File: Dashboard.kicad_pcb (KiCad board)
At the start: 2 copper layers, 176.5 x 121.5 mm, 160 parts, among them J1 Left_Signal, J10 AccelConn, J11 BrakeConn, J12 AccelConn2, J13 BrakeConn2, J14 Motor-P, J15 Motor-C, J16 Array-C, J17 Array-P, J18 PowerConn, J19 CAN_OUT, J2 Right_Signal, J20 MotorCANConnector, J21 CAN_IN, J22 CAN_OUT, J23 USB_B_Micro, J24 ExtraGPIO_Conn, J25 UART_TP, J26 CAN_TP, J27 CAN_TP, J3 Brake Light, J4 Headlight, J5 MinionConn, J6 SPI, J7 BPS_PWR, J8 JTAG, SW10 RESET, SW8 SW_Rotary2x6, SW9 KILL_SW, U1 EL3H7, U10 EL3H7, U11 EL3H7, U12 RI3-1205S, U13 NCP1117-3.3_SOT223, U14 ADM3055E, U15 CDSOT23-T24CAN, U16 LTC6820, U17 ADM3055E, U18 CDSOT23-T24CAN, U19 CP2102N-A01-GQFN24, U2 EL3H7, U20 HX1188FNL, U3 EL3H7, U4 EL3H7, U5 EL3H7, U6 EL3H7, U7 STM32F413RHTx, U8 EL3H7, U9 EL3H7, Y1 Crystal

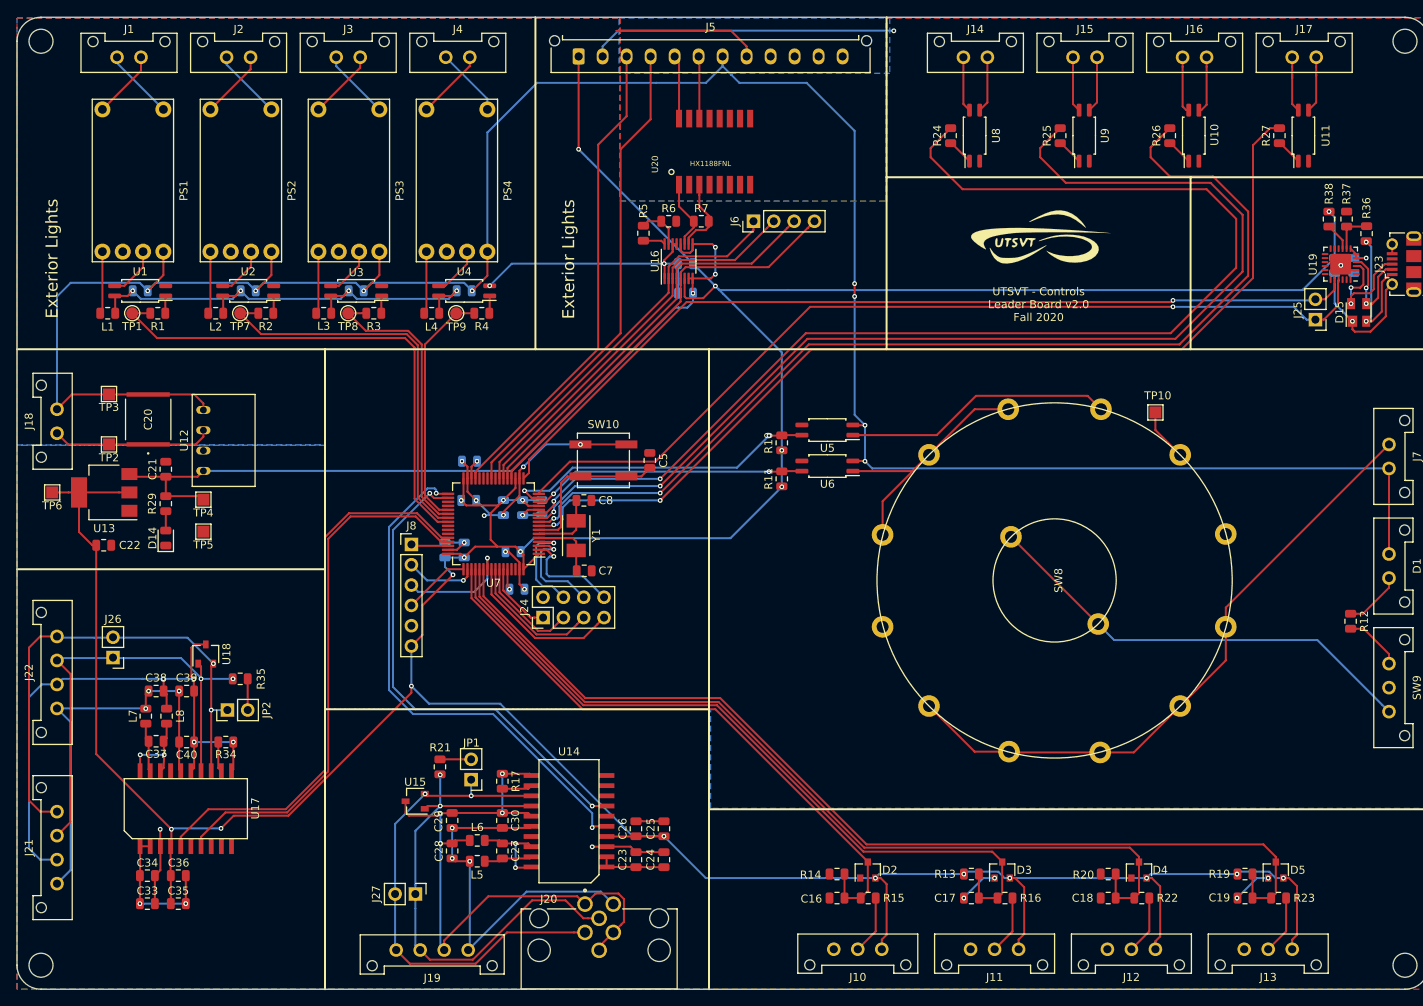
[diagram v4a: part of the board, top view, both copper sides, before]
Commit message: Labels sections and fixes DRC errors
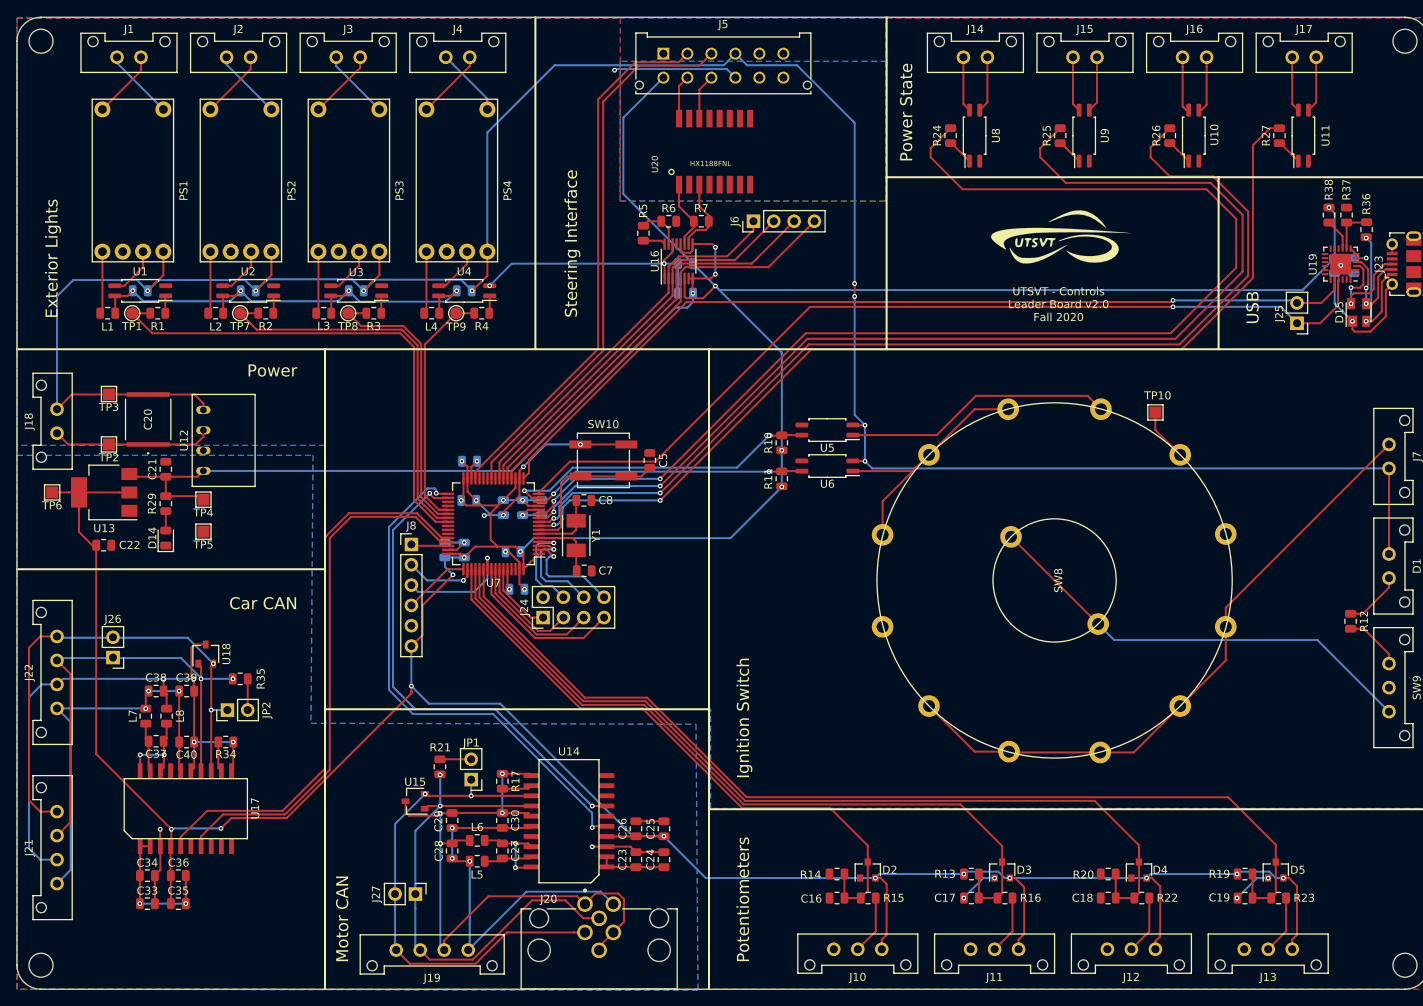
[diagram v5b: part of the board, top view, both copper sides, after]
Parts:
- J5: footprint Connector_Molex:Molex_Micro-Fit_3.0_43650-1215_1x12_P3.00mm_Vertical -> UTSVT_Connectors:Molex_MicroFit3.0_2x6xP3.00mm_PolarizingPeg_Vertical
- moved J5 10.6 mm to (111.8, 58.0)
- moved LOGO2 2.50 mm to (161.2, 81.1)
- moved J25 2.34 mm to (191.0, 91.8)
- moved R36 0.50 mm to (199.7, 80.0)
- moved R37 0.50 mm to (197.2, 78.2)
- moved R38 0.50 mm to (195.0, 78.2)
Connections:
- J5 pad 1: +3V3 -> +12V
- J5 pad 10: Net-(J5-Pad10) -> GND
- J5 pad 2: +12V -> /UART3_Tx
- J5 pad 3: /UART3_Tx -> /UART3_Rx
- J5 pad 4: /UART3_Rx -> GNDPWR
- J5 pad 7: GNDPWR -> +3V3
- J5 pad 8: GND -> Net-(J5-Pad8)
- U20 pad 14: Net-(J5-Pad6) -> Net-(J5-Pad9)
- U20 pad 16: Net-(J5-Pad5) -> Net-(J5-Pad8)
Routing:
- net +12V: track 120.3 -> 82.6 mm, vias 5 -> 4
- net Net-(J5-Pad5): track 8.00 -> 0.00 mm
- net /UART3_Rx: track 61.0 -> 68.9 mm
- net Net-(J5-Pad6): track 7.81 -> 0.00 mm
- net /UART3_Tx: track 60.6 -> 67.3 mm
- net Net-(J5-Pad9): track 0.00 -> 5.75 mm
- net Net-(J5-Pad8): track 0.00 -> 5.56 mm
- net GND: track 163.4 -> 160.6 mm, vias 20 -> 21
- net +3V3: track 533.1 -> 530.5 mm, vias 22 -> 21
- net GNDPWR: track 303.2 -> 305.2 mm
- net /Accel_Pot: track 76.7 -> 78.0 mm
- net /Brake_Pot: track 93.2 -> 94.4 mm
- net /Brake_Pot2: track 126.6 -> 127.5 mm
- net /Accel_Pot2: track 110.1 -> 111.0 mm
- net Net-(R38-Pad2): track 3.46 -> 3.96 mm
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- removed copper zone on B.Cu, net (none)
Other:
- net class Default: clearance 0.2 -> 0.127
- rule trace_clearance: 0.2 -> 0.127
- board text added: "Car CAN"
- board text added: "Ignition Switch"
- board text added: "Motor CAN"
- board text added: "Potentiometers"
- board text added: "Power"
- board text added: "Power State"
- board text added: "Steering Interface"
- board text added: "USB"

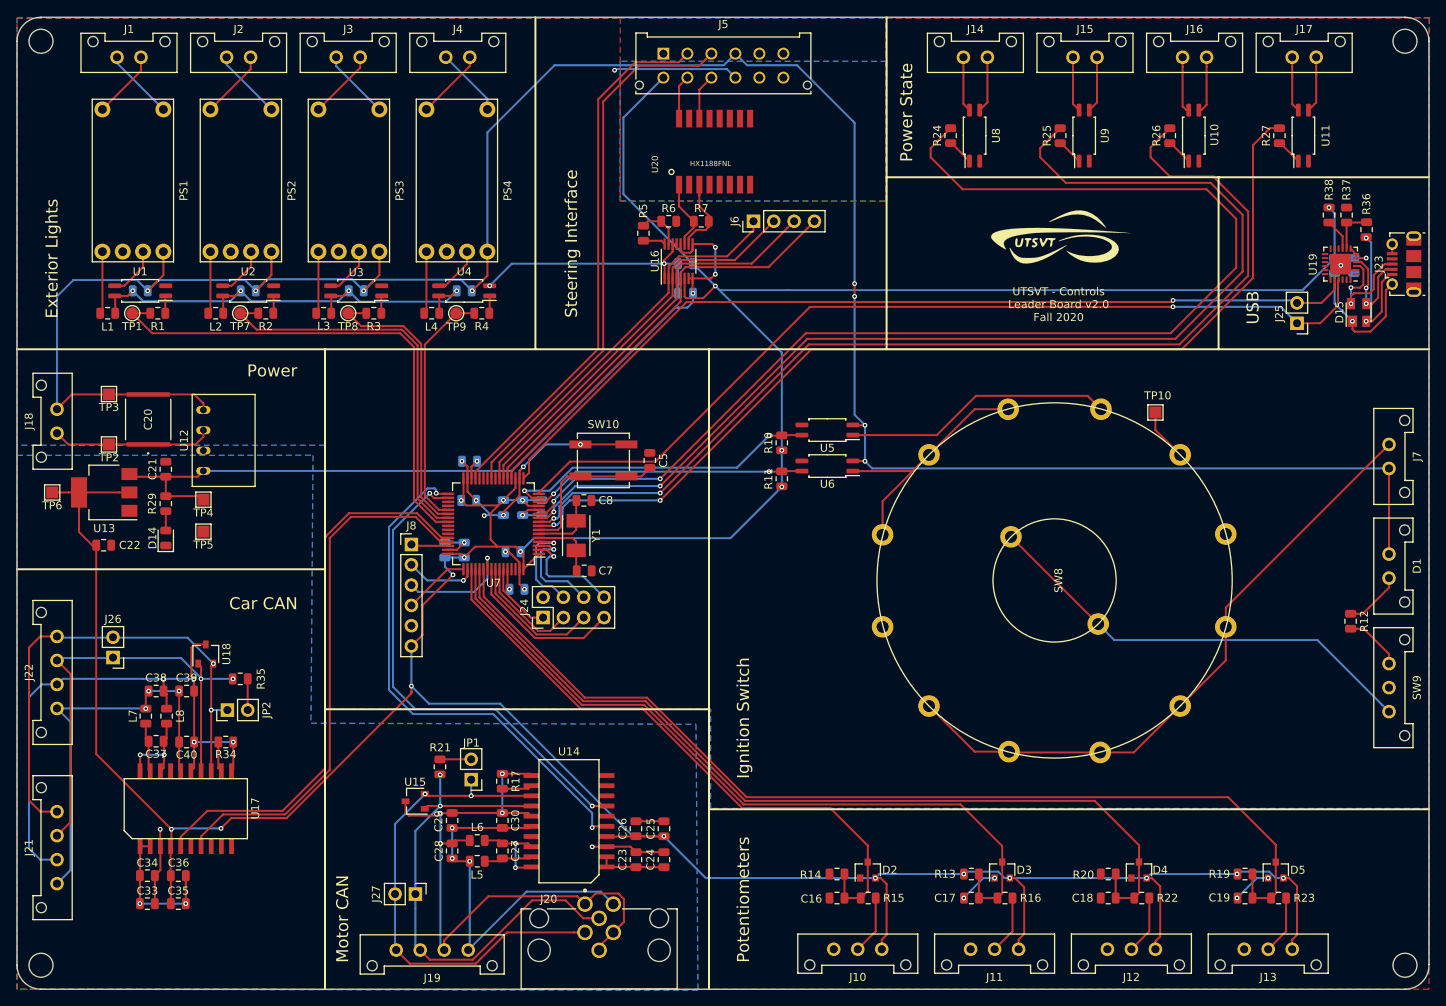
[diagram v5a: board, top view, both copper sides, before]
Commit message: Adds labels to some connectors and edits layout to meet 0,2mm pad to trace clearance
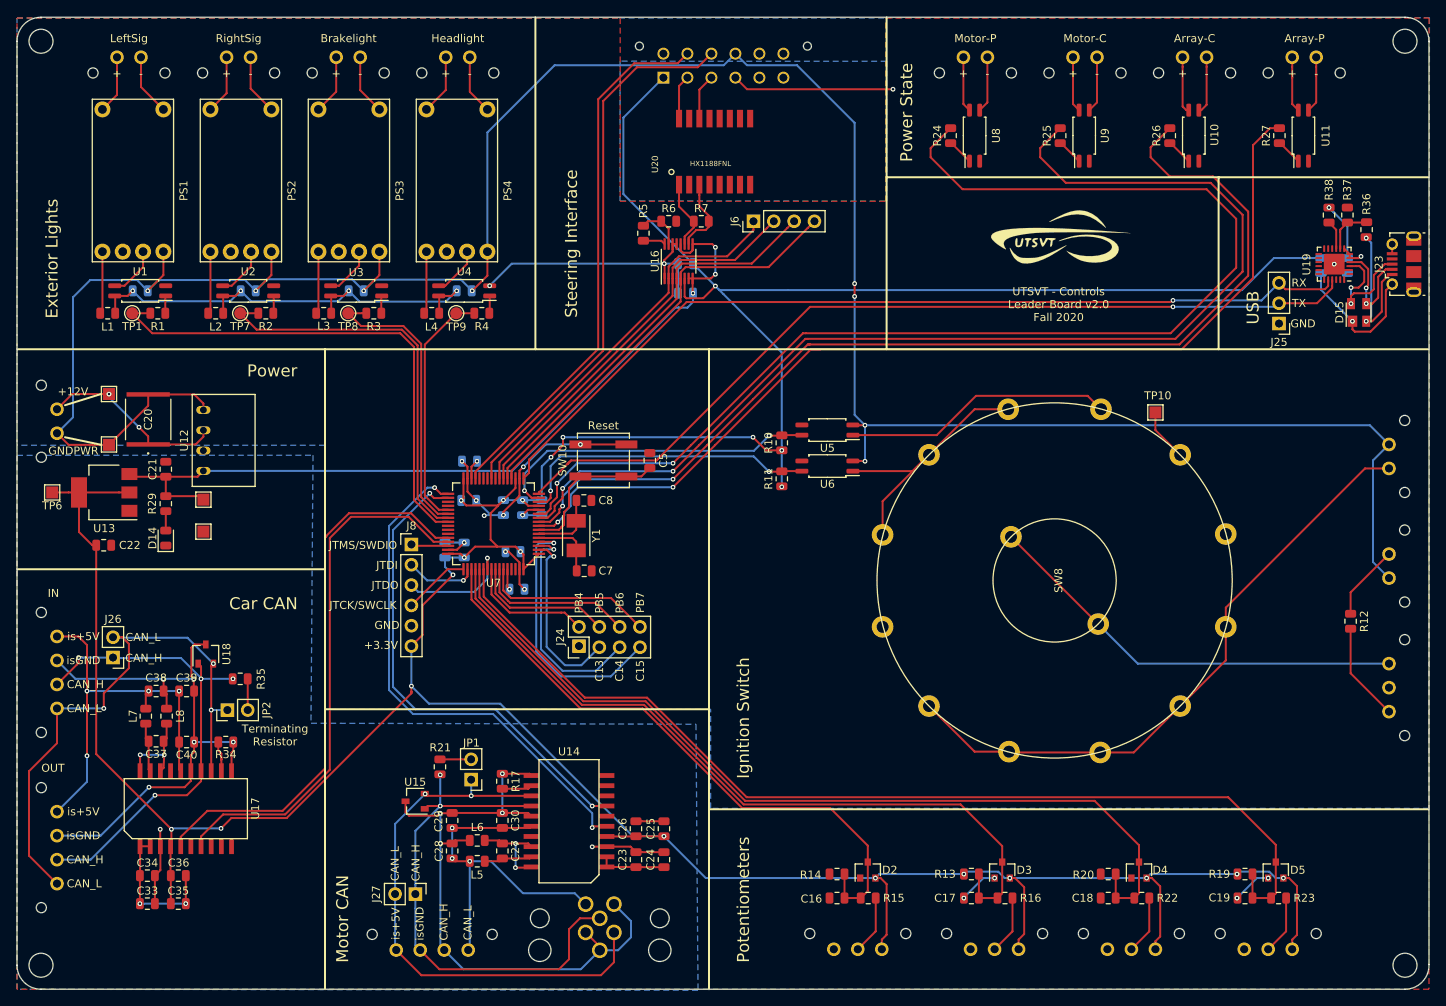
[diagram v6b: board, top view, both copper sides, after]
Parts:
- D1, J1, J10, J11, J12, J13, J14, J15, J16, J17, J18, J19, J2, J20, J21, J22, J3, J4, J5, J7, SW9: moved to B.Cu
- J25: footprint Connector_PinHeader_2.54mm:PinHeader_1x02_P2.54mm_Vertical -> Connector_PinHeader_2.54mm:PinHeader_1x03_P2.54mm_Vertical
- moved LOGO1 69.7 mm to (160.5, 86.5), turned to 270 degrees
- moved J21 9.00 mm to (36.0, 152.8), turned to 270 degrees
- moved J22 9.00 mm to (36.0, 130.9), turned to 270 degrees
- moved TP2 6.30 mm to (42.5, 100.6)
- moved TP3 6.30 mm to (42.5, 106.9)
- moved SW9 6.00 mm to (202.5, 140.3), turned to 90 degrees
- moved J24 5.82 mm to (101.2, 132.2)
- moved J20 3.12 mm to (102.2, 194.2), turned to 180 degrees
- moved D1 3.00 mm to (202.5, 123.6), turned to 90 degrees
- moved J18 3.00 mm to (36.0, 102.5), turned to 270 degrees
- moved J5 3.00 mm to (111.8, 61.0)
- moved J7 3.00 mm to (202.5, 109.9), turned to 90 degrees
- moved J25 2.25 mm to (188.8, 91.8)
- moved C42 1.70 mm to (194.0, 84.5)
- moved C41 0.80 mm to (197.3, 84.5)
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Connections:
- J24 pad 1: /PB7 -> GND
- J24 pad 2: Net-(J24-Pad2) -> /PB4
- J24 pad 3: /PB6 -> /PC13
- J24 pad 4: /PC15 -> /PB5
- J24 pad 5: /PB5 -> /PC14
- J24 pad 6: /PC14 -> /PB6
- J24 pad 7: /PB4 -> /PC15
- J24 pad 8: /PC13 -> /PB7
- J25 pad 1: /UART2_Tx -> GND
- J25 pad 2: /UART2_Rx -> /UART2_Tx
- J5 pad 1: +12V -> +3V3
- J5 pad 10: GND -> GNDPWR
- J5 pad 2: /UART3_Tx -> Net-(J5-Pad2)
- J5 pad 3: /UART3_Rx -> Net-(J5-Pad3)
- J5 pad 4: GNDPWR -> GND
- J5 pad 7: +3V3 -> +12V
- J5 pad 8: Net-(J5-Pad8) -> /UART3_Tx
- J5 pad 9: Net-(J5-Pad9) -> /UART3_Rx
- PS1 pad 5: Net-(J1-Pad1) -> Net-(J1-Pad2)
- PS1 pad 6: Net-(J1-Pad2) -> Net-(J1-Pad1)
- PS2 pad 5: Net-(J2-Pad1) -> Net-(J2-Pad2)
- PS2 pad 6: Net-(J2-Pad2) -> Net-(J2-Pad1)
- PS3 pad 5: Net-(J3-Pad1) -> Net-(J3-Pad2)
- PS3 pad 6: Net-(J3-Pad2) -> Net-(J3-Pad1)
- PS4 pad 5: Net-(J4-Pad1) -> Net-(J4-Pad2)
- PS4 pad 6: Net-(J4-Pad2) -> Net-(J4-Pad1)
- U20 pad 14: Net-(J5-Pad9) -> Net-(J5-Pad3)
- U20 pad 16: Net-(J5-Pad8) -> Net-(J5-Pad2)
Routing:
- net /PC15: track 12.8 -> 33.3 mm
- net /PC14: track 13.3 -> 28.1 mm
- net GNDPWR: track 305.2 -> 318.4 mm
- net /PB7: track 9.05 -> 21.6 mm
- net /PC13: track 13.5 -> 22.6 mm
- net /Car_CAN/CAN_L: track 63.9 -> 71.7 mm, vias 2 -> 3
- net GND: track 160.6 -> 168.0 mm
- net /Motor_CAN/CAN_L: track 62.5 -> 69.5 mm
- net /PB6: track 13.6 -> 19.7 mm
- net Net-(J5-Pad9): track 5.75 -> 0.00 mm
- net Net-(J5-Pad3): track 0.00 -> 5.75 mm
- net Net-(C38-Pad2): track 74.8 -> 69.1 mm, vias 4 -> 5
- net Net-(J5-Pad8): track 5.56 -> 0.00 mm
- net Net-(J5-Pad2): track 0.00 -> 5.56 mm
- net Net-(C28-Pad1): track 49.1 -> 44.0 mm
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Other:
- net class Default: clearance 0.127 -> 0.2
- rule trace_clearance: 0.127 -> 0.2
- board text added: "+"
- board text added: "+12V"
- board text added: "+3.3V"
- board text added: "-"
- board text added: "Array-C"
- board text added: "Array-P"
- board text added: "Brakelight"
- board text added: "C13"
- board text added: "C14"
- board text added: "C15"
- board text added: "CAN_H"
- board text added: "CAN_L"
- board text added: "GND"
- board text added: "GNDPWR"
- board text added: "Headlight"
- board text added: "IN"
- board text added: "JTCK/SWCLK"
- board text added: "JTDI"
- board text added: "JTDO"
- board text added: "JTMS/SWDIO"
- board text added: "LeftSig"
- board text added: "Motor-C"
- board text added: "Motor-P"
- board text added: "OUT"
- board text added: "PB4"
- board text added: "PB5"
- board text added: "PB6"
- board text added: "PB7"
- board text added: "RX"
- board text added: "Reset"
- board text added: "RightSig"
- board text added: "TX"
- board text added: "Terminating Resistor"
- board text added: "i5"
- board text added: "iG"
- board text added: "is+5V"
- board text added: "isGND"
